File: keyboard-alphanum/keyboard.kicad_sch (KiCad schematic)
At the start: 85 parts, among them J1 BOOT0, J2 BOOT1, J3 ST-Link, J4 USB_B_Mini, J5 USB_A, J6 USB_A, J7 USB_A, J8 UART, SW1 NL, SW10 plus, SW11 2, SW12 sub, SW13 4, SW14 3, SW15 7, SW16 5, SW17 enter, SW2 8, SW3 6, SW4 0, SW5 div, SW6 9, SW7 1, SW8 dot, SW9 mul, U1 STM32F103C6T6A, U2 LD1117S33TR, U3 HS8836A, Y1 8MHz, Y2 32768MHz

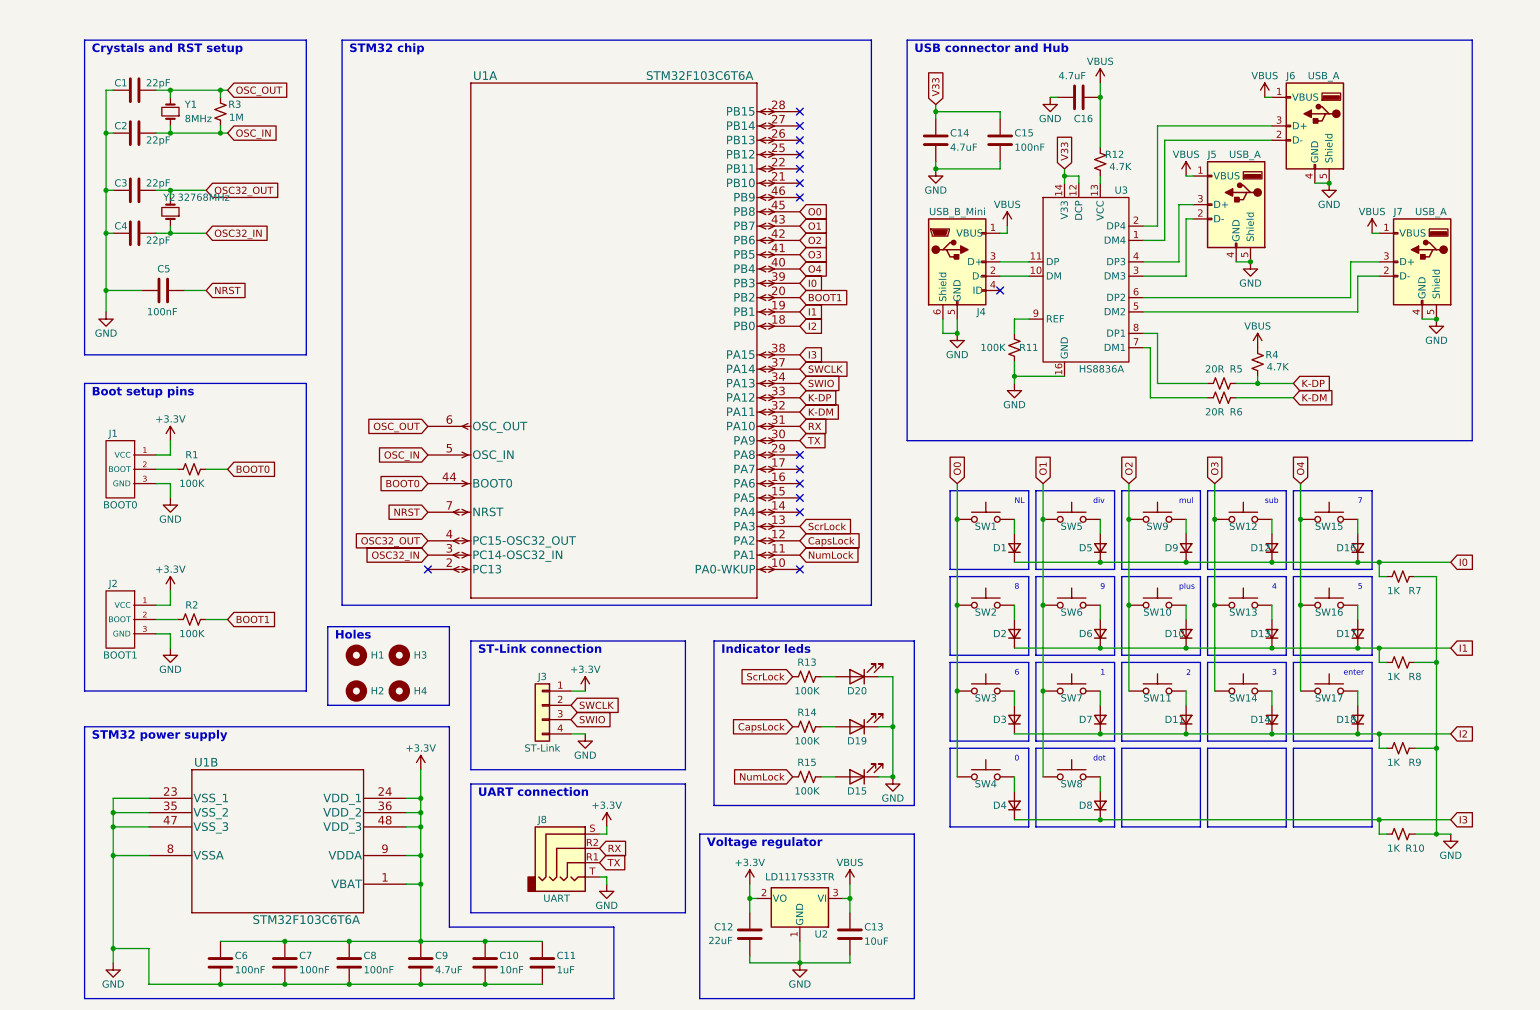
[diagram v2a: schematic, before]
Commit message: Fix issues and update alphanum keyboard
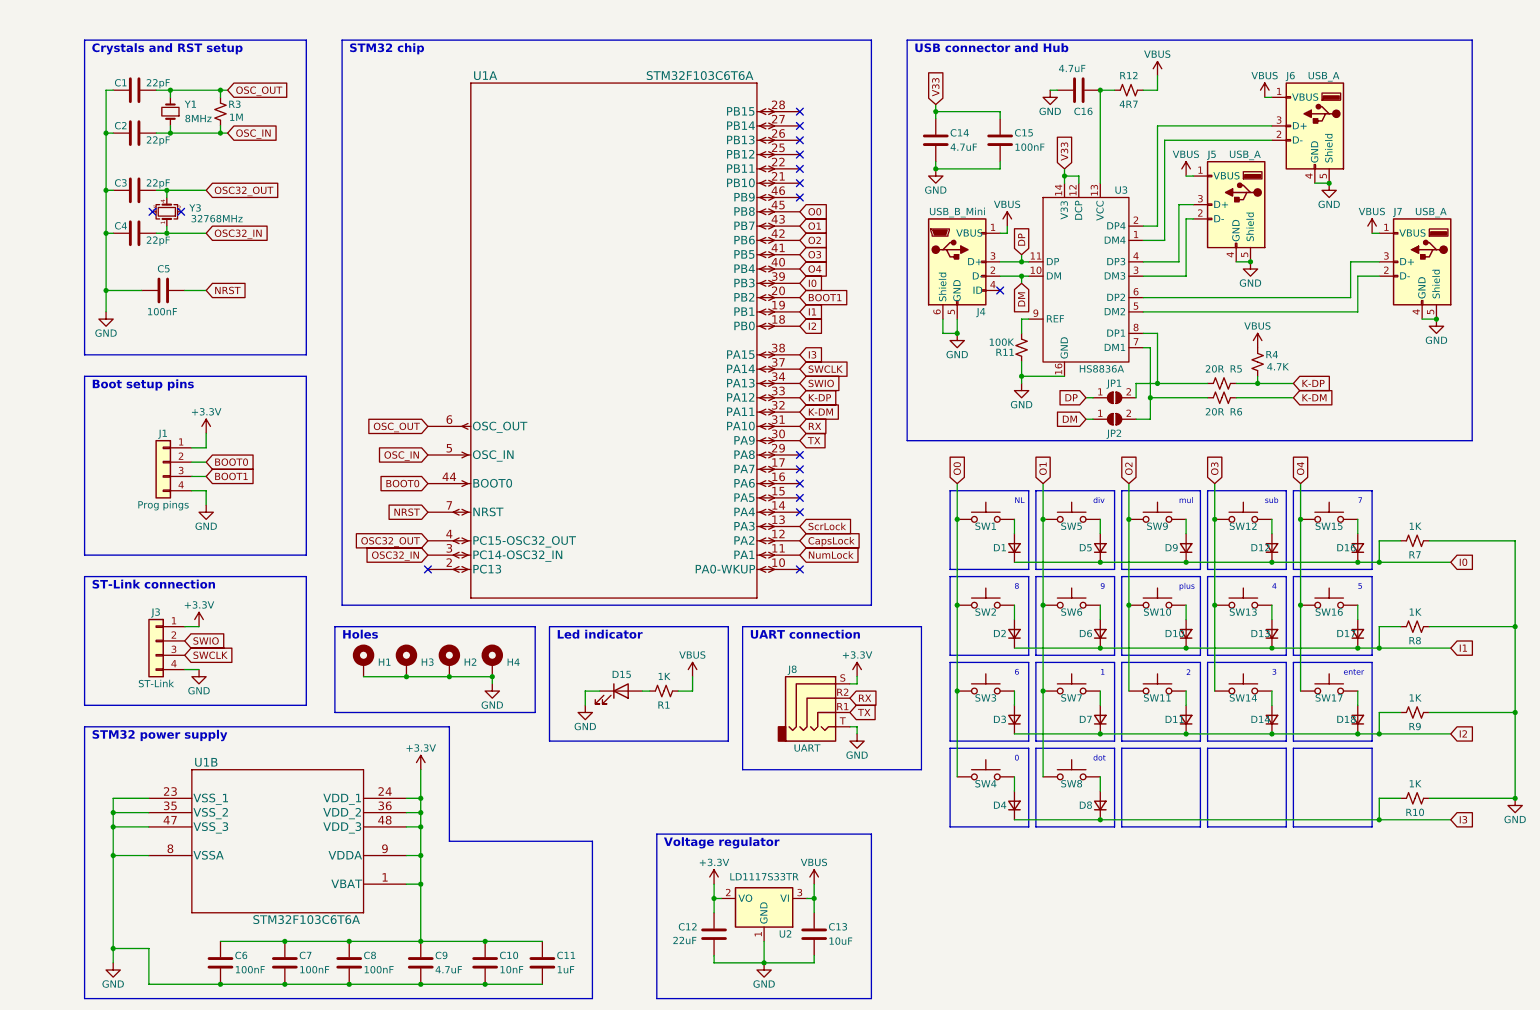
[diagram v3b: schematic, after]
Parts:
- removed D19: CapsLock, LED_THT:LED_D5.0mm, symbol Device:LED
- removed D20: ScrollLock, LED_THT:LED_D5.0mm, symbol Device:LED
- removed J1: BOOT0, Jumper:SolderJumper-3_P1.3mm_Open_RoundedPad1.0x1.5mm, symbol symbols:boot_pins
- removed J2: BOOT1, Jumper:SolderJumper-3_P1.3mm_Open_RoundedPad1.0x1.5mm, symbol symbols:boot_pins
- removed R13, R14, R15, R2: 100K, Resistor_SMD:R_0805_2012Metric, symbol Device:R_Small_US
- removed Y2: 32768MHz, Crystal:Crystal_SMD_SeikoEpson_MC306-4Pin_8.0x3.2mm, symbol Device:Crystal_Small
- added J1: Prog pings, Connector_PinHeader_2.54mm:PinHeader_1x04_P2.54mm_Vertical, symbol Connector_Generic:Conn_01x04
- added JP1, JP2: SolderJumper_2_Open, Jumper:SolderJumper-2_P1.3mm_Open_RoundedPad1.0x1.5mm, symbol Jumper:SolderJumper_2_Open
- added Y3: 32768MHz, Crystal:Crystal_SMD_SeikoEpson_MC306-4Pin_8.0x3.2mm, symbol Device:Crystal_GND23_Small
- D15: value NumLock -> LED; footprint LED_THT:LED_D5.0mm -> LED_SMD:LED_0805_2012Metric
- H1, H2, H3, H4: footprint (none) -> MountingHole:MountingHole_3.2mm_M3_DIN965_Pad; symbol Mechanical:MountingHole -> Mechanical:MountingHole_Pad
- R1: value 100K -> 1K
- R12: value 4.7K -> 4R7
- U1: footprint (none) -> Package_QFP:LQFP-48_7x7mm_P0.5mm
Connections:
- net +3.3V: now also J1.1 (Pin_1)
- net BOOT0: now also J1.2 (Pin_2); no longer R1.2
- net BOOT1: now also J1.3 (Pin_3)
- net GND: now also H1.1, H2.1, H3.1, H4.1, J1.4 (Pin_4)
- net OSC32_IN: now also Y3.1
- net OSC32_OUT: now also Y3.4
- net SWCLK: now also J3.3 (Pin_3); no longer J3.2 (Pin_2)
- net SWIO: now also J3.2 (Pin_2); no longer J3.3 (Pin_3)
- net VBUS: now also R1.2; no longer C16.2
- net DM: now reaches J4.2 (D-), U3.10 (DM)
- net DM: now also JP2.1 (A)
- net DP: now reaches J4.3 (D+), U3.11 (DP)
- net DP: now also JP1.1 (A)
- net at R12.1, U3.13 (VCC): now also C16.2
- net at R6.1, U3.7 (DM1): now also JP2.2 (B)
- net at R5.1, U3.8 (DP1): now also JP1.2 (B)
- net at R1.1: now also D15.2 (A)
- no-connect marks 15 -> 17
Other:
- note added: "Led indicator"
- note removed: "Indicator leds"
- moved on the sheet: C12, C13, C16, J3, J8, R10, R11, R12, R7, R8, R9, U2
